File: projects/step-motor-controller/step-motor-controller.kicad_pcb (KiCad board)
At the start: 2 copper layers, 100 x 80 mm, 34 parts, among them J1 Terminal_3P, J2 Motor_4P, J3 Encoder_8P, Q1 BC547, SW1 Limit_SW, SW2 Limit_SW, U1 OKI-78SR-5, U2 UART_4P, U3 ESP32-DevKitC, U4 LV8729, U5 AM26LS32ACN, U6 74HC4050

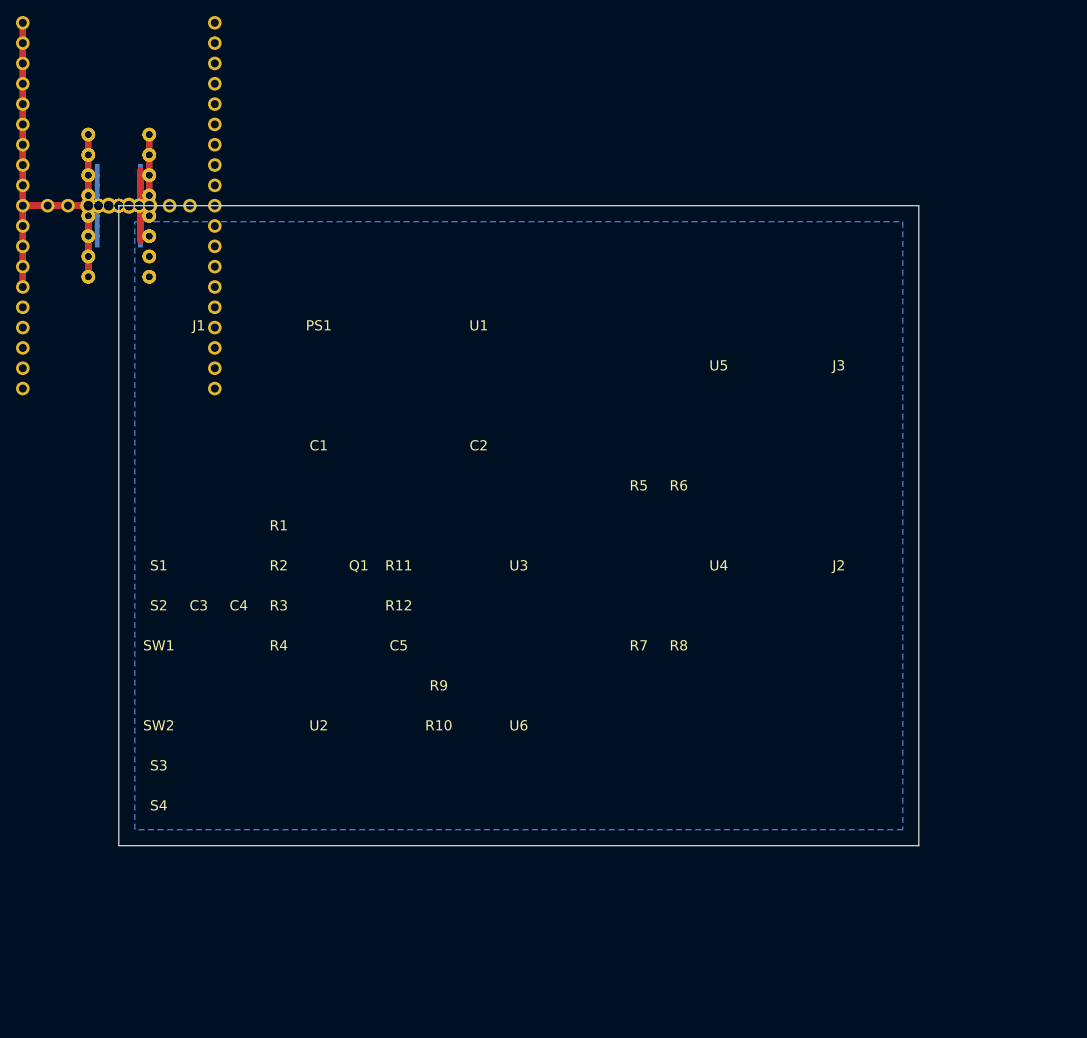
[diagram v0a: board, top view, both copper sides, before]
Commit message: feat: verified Step Motor Controller — 45-net schematic match, routed PCB, 0 electrical DRC, fab package
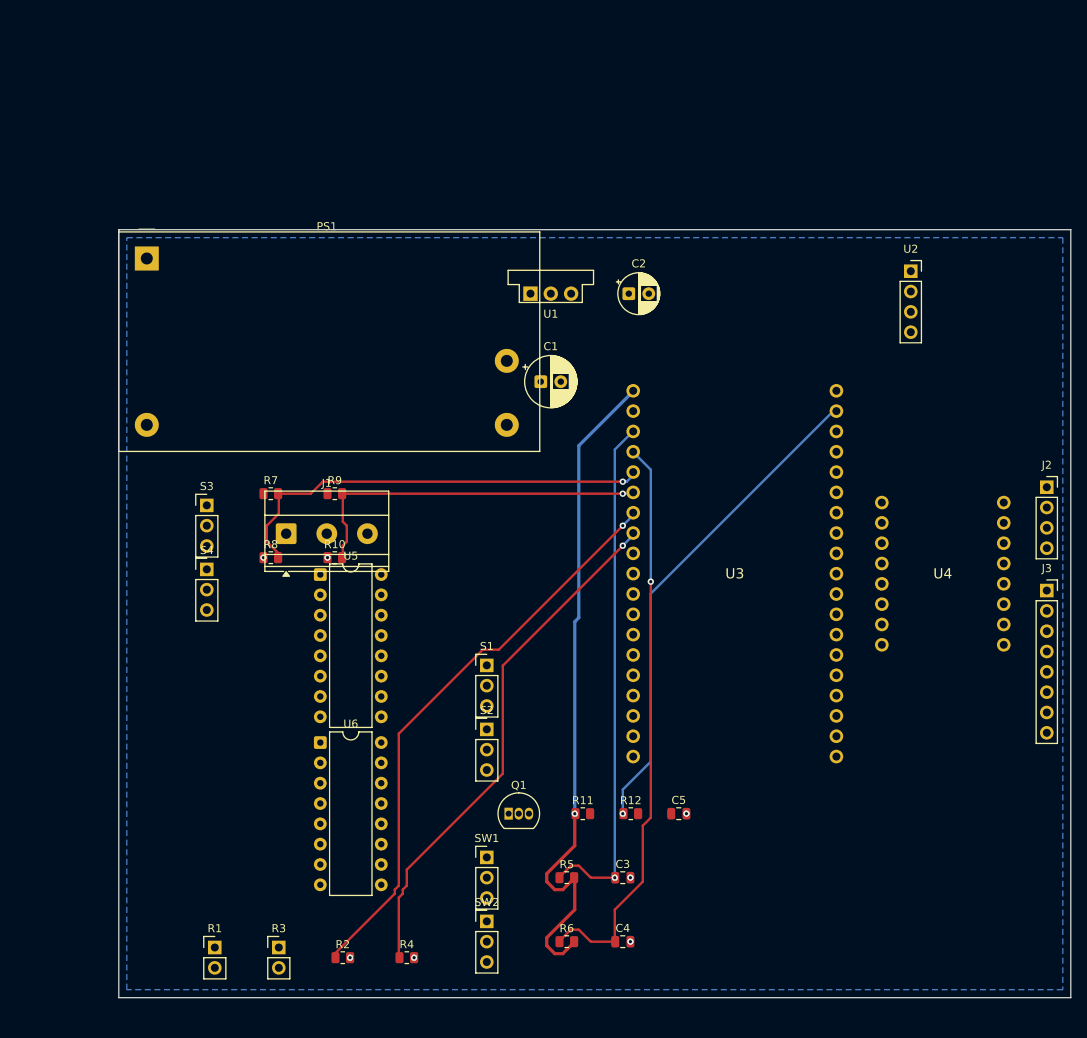
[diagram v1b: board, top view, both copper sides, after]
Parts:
- C1: value 100uF -> C1; footprint (none) -> CP_Radial_D6.3mm_P2.50mm
- C2: value 10uF -> C2; footprint (none) -> CP_Radial_D5.0mm_P2.50mm
- C3: value 100nF -> C3; footprint (none) -> C_0805_2012Metric
- C4: value 100nF -> C4; footprint (none) -> C_0805_2012Metric
- C5: value 100nF -> C5; footprint (none) -> C_0805_2012Metric
- J1: value Terminal_3P -> AC Input; footprint (none) -> TerminalBlock_Phoenix_MKDS-1,5-3-5.08_1x03_P5.08mm_Horizontal
- J2: value Motor_4P -> Motor; footprint (none) -> PinSocket_1x04_P2.54mm_Vertical
- J3: value Encoder_8P -> Encoder; footprint (none) -> PinSocket_1x08_P2.54mm_Vertical
- PS1: footprint (none) -> Converter_ACDC_MeanWell_IRM-20-xx_THT
- Q1: footprint (none) -> TO-92_Inline
- R1: value 10K -> R1; footprint (none) -> PinHeader_1x02_P2.54mm_Vertical
- R10: value 4.7K -> R10; footprint (none) -> R_0805_2012Metric
- R11: value 10K -> R11; footprint (none) -> R_0805_2012Metric
- R12: value 1K -> R12; footprint (none) -> R_0805_2012Metric
- R2: value 10K -> R2; footprint (none) -> R_0805_2012Metric
- R3: value 10K -> R3; footprint (none) -> PinHeader_1x02_P2.54mm_Vertical
- R4: value 10K -> R4; footprint (none) -> R_0805_2012Metric
- R5: value 1K -> R5; footprint (none) -> R_0805_2012Metric
- R6: value 1K -> R6; footprint (none) -> R_0805_2012Metric
- R7: value 10K -> R7; footprint (none) -> R_0805_2012Metric
- R8: value 10K -> R8; footprint (none) -> R_0805_2012Metric
- R9: value 4.7K -> R9; footprint (none) -> R_0805_2012Metric
- S1: value Optical -> S1; footprint (none) -> PinHeader_1x03_P2.54mm_Vertical
- S2: value Optical -> S2; footprint (none) -> PinHeader_1x03_P2.54mm_Vertical
- S3: value Hall -> S3; footprint (none) -> PinHeader_1x03_P2.54mm_Vertical
- S4: value Hall -> S4; footprint (none) -> PinHeader_1x03_P2.54mm_Vertical
- SW1: value Limit_SW -> SW1; footprint (none) -> PinHeader_1x03_P2.54mm_Vertical
- SW2: value Limit_SW -> SW2; footprint (none) -> PinHeader_1x03_P2.54mm_Vertical
- U1: footprint (none) -> Converter_DCDC_Murata_OKI-78SR_Vertical
- U2: value UART_4P -> UART Display; footprint (none) -> PinSocket_1x04_P2.54mm_Vertical
- U5: footprint (none) -> DIP-16_W7.62mm
- U6: value 74HC4050 -> 74HC4050N; footprint (none) -> DIP-16_W7.62mm
- moved U2 93.3 mm to (99.0, 8.19)
- moved C4 63.8 mm to (63.0, 92.0)
- moved C3 63.0 mm to (63.0, 84.0)
- moved R6 58.7 mm to (56.0, 92.0)
- moved U5 56.2 mm to (25.2, 46.1)
- moved R1 53.3 mm to (12.0, 92.7)
- moved R8 52.2 mm to (19.0, 44.0)
- moved R5 49.8 mm to (56.0, 84.0)
- moved R7 49.8 mm to (19.0, 36.0)
- moved R2 49.6 mm to (28.0, 94.0)
- moved SW1 48.8 mm to (46.0, 81.5)
- moved SW2 47.7 mm to (46.0, 89.5)
- moved S2 43.8 mm to (46.0, 65.5)
- moved S1 42.9 mm to (46.0, 57.5)
- moved R3 42.7 mm to (20.0, 92.7)
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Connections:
- C3 pad 1: (no net) -> SW1_SIG
- C3 pad 2: (no net) -> GND
- C4 pad 1: (no net) -> SW2_SIG
- C4 pad 2: (no net) -> GND
- C5 pad 1: (no net) -> CHIP_PU
- C5 pad 2: (no net) -> GND
- J1 pad 1: (no net) -> AC_L
- J1 pad 2: (no net) -> AC_N
- J2 pad 1: (no net) -> MOT_1A
- J2 pad 2: (no net) -> MOT_1B
- J2 pad 3: (no net) -> MOT_2A
- J2 pad 4: (no net) -> MOT_2B
- J3 pad 3: (no net) -> ENC_A_P
- J3 pad 4: (no net) -> ENC_A_N
- J3 pad 5: (no net) -> ENC_B_P
- J3 pad 6: (no net) -> ENC_B_N
- J3 pad 7: (no net) -> ENC_Z_P
- J3 pad 8: (no net) -> ENC_Z_N
- PS1 pad 1: (no net) -> AC_L
- PS1 pad 2: (no net) -> AC_N
- Q1 pad 1: (no net) -> CHIP_PU
- Q1 pad 2: (no net) -> Q1_BASE
- Q1 pad 3: (no net) -> GND
- R1 pad 2: (no net) -> FSR1_TOP
- R10 pad 1: (no net) -> GND
- R10 pad 2: (no net) -> HALL2_DIV
- R11 pad 2: (no net) -> CHIP_PU
- R12 pad 1: (no net) -> GPIO23_RST
- R12 pad 2: (no net) -> Q1_BASE
- R2 pad 1: (no net) -> FSR1_TOP
- R2 pad 2: (no net) -> GND
- R3 pad 2: (no net) -> FSR2_TOP
- R4 pad 1: (no net) -> FSR2_TOP
- R4 pad 2: (no net) -> GND
- R5 pad 1: (no net) -> SW1_SIG
- R6 pad 1: (no net) -> SW2_SIG
- R7 pad 1: (no net) -> HALL1_RAW
- R7 pad 2: (no net) -> HALL1_DIV
- R8 pad 1: (no net) -> GND
- R8 pad 2: (no net) -> HALL1_DIV
- R9 pad 1: (no net) -> HALL2_RAW
- R9 pad 2: (no net) -> HALL2_DIV
- S1 pad 2: (no net) -> OPTIC1_RAW
- S1 pad 3: (no net) -> GND
- S2 pad 2: (no net) -> OPTIC2_RAW
- S2 pad 3: (no net) -> GND
- S3 pad 2: (no net) -> GND
- S3 pad 3: GND -> HALL1_RAW
- S4 pad 2: (no net) -> GND
- S4 pad 3: GND -> HALL2_RAW
- SW1 pad 1: (no net) -> SW1_SIG
- SW1 pad 2: (no net) -> GND
- SW1 pad 3: GND -> (no net)
- SW2 pad 1: (no net) -> SW2_SIG
- SW2 pad 2: (no net) -> GND
- SW2 pad 3: GND -> (no net)
- U2 pad 2: (no net) -> UART_M_TX
- U2 pad 3: (no net) -> UART_M_RX
- U3 pad 10: (no net) -> M_STEP
- U3 pad 11: (no net) -> M_DIR
- U3 pad 12: (no net) -> M_EN
- U3 pad 15: (no net) -> ENC_Z_ESP
- U3 pad 19: (no net) -> +5V
- U3 pad 2: (no net) -> CHIP_PU
- U3 pad 26: (no net) -> M_MS1
- U3 pad 27: (no net) -> UART_M_TX
- U3 pad 28: (no net) -> UART_M_RX
- U3 pad 29: (no net) -> M_MS2
- U3 pad 3: (no net) -> SW1_SIG
- U3 pad 30: (no net) -> GPIO18_OPTIC1
- U3 pad 31: (no net) -> GPIO19_OPTIC2
- U3 pad 32: (no net) -> GPIO21_ENC_A
- U3 pad 33: (no net) -> GPIO22_ENC_B
- U3 pad 37: (no net) -> GPIO23_RST
- U3 pad 4: (no net) -> SW2_SIG
- U3 pad 5: (no net) -> HALL1_DIV
- U3 pad 6: (no net) -> HALL2_DIV
- U3 pad 7: (no net) -> FSR1_TOP
- U3 pad 8: (no net) -> FSR2_TOP
- U3 pad 9: (no net) -> M_MS3
- U4 pad 1: (no net) -> M_EN
- U4 pad 11: (no net) -> MOT_2B
- U4 pad 12: (no net) -> MOT_2A
- U4 pad 13: (no net) -> MOT_1B
- U4 pad 14: (no net) -> MOT_1A
- U4 pad 2: (no net) -> M_MS1
- U4 pad 3: (no net) -> M_MS2
- U4 pad 4: (no net) -> M_MS3
- U4 pad 7: (no net) -> M_STEP
- U4 pad 8: (no net) -> M_DIR
- U5 pad 1: (no net) -> ENC_A_N
- U5 pad 10: (no net) -> ENC_Z_N
- U5 pad 11: (no net) -> ENC_Z_BUF
- U5 pad 2: (no net) -> ENC_A_P
- U5 pad 3: (no net) -> ENC_A_BUF
- U5 pad 5: (no net) -> ENC_B_BUF
- U5 pad 6: (no net) -> ENC_B_N
- U5 pad 7: (no net) -> ENC_B_P
- U5 pad 9: (no net) -> ENC_Z_P
- U6 pad 10: (no net) -> GPIO18_OPTIC1
- U6 pad 11: (no net) -> OPTIC2_RAW
- U6 pad 12: (no net) -> GPIO19_OPTIC2
- U6 pad 2: (no net) -> GPIO21_ENC_A
- U6 pad 3: (no net) -> ENC_A_BUF
- U6 pad 4: (no net) -> GPIO22_ENC_B
- U6 pad 5: (no net) -> ENC_B_BUF
- U6 pad 6: (no net) -> ENC_Z_ESP
- U6 pad 7: (no net) -> ENC_Z_BUF
- U6 pad 9: (no net) -> OPTIC1_RAW
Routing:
- net GND: track 100.0 -> 0.00 mm, vias 0 -> 7
- net +5V: track 80.8 -> 0.00 mm
- net FSR1_TOP: track 0.00 -> 72.2 mm, vias 0 -> 1
- net SW2_SIG: track 0.00 -> 71.9 mm, vias 0 -> 1
- net SW1_SIG: track 0.00 -> 65.3 mm, vias 0 -> 1
- net FSR2_TOP: track 0.00 -> 65.2 mm, vias 0 -> 1
- net GPIO23_RST: track 0.00 -> 61.5 mm, vias 0 -> 1
- net HALL1_DIV: track 0.00 -> 54.8 mm, vias 0 -> 1
- net +3V3: track 37.9 -> 85.1 mm, vias 0 -> 1
- net HALL2_DIV: track 0.00 -> 44.9 mm, vias 0 -> 1
- net +24V: track 17.3 -> 0.00 mm
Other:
- board size 100 x 80 mm -> 119 x 96 mm

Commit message: feat: THT PCB - routed, 0 electrical DRC, 0 parity, Gerber+drill+BOM+PnP+renders
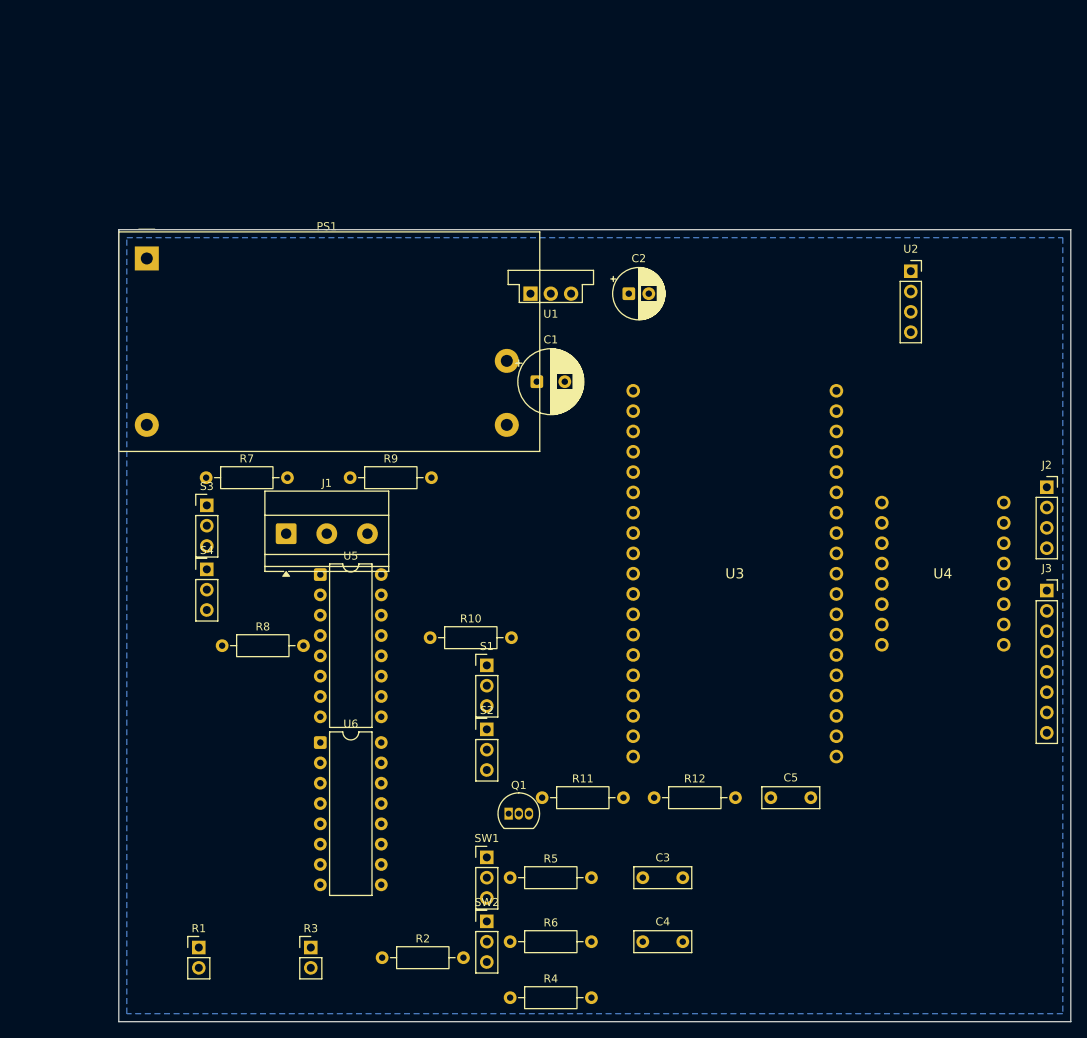
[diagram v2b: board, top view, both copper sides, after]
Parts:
- C1: footprint CP_Radial_D6.3mm_P2.50mm -> CP_Radial_D8.0mm_P3.50mm
- C2: footprint CP_Radial_D5.0mm_P2.50mm -> CP_Radial_D6.3mm_P2.50mm
- C3, C4, C5: footprint C_0805_2012Metric -> C_Rect_L7.0mm_W2.5mm_P5.00mm
- R10, R11, R12, R2, R4, R5, R6, R7, R8, R9: footprint R_0805_2012Metric -> R_Axial_DIN0207_L6.3mm_D2.5mm_P10.16mm_Horizontal
- moved R10 15.6 mm to (38.9, 54.0)
- moved R4 13.9 mm to (48.9, 99.0)
- moved R8 12.6 mm to (12.9, 55.0)
- moved C5 11.7 mm to (81.5, 74.0)
- moved R7 8.32 mm to (10.9, 34.0)
- moved R5 7.08 mm to (48.9, 84.0)
- moved R6 7.08 mm to (48.9, 92.0)
- moved R11 5.46 mm to (52.9, 74.0)
- moved R2 4.92 mm to (32.9, 94.0)
- moved R3 4.00 mm to (24.0, 92.7)
- moved R12 3.54 mm to (66.9, 74.0)
- moved R9 2.77 mm to (28.9, 34.0)
- moved C3 2.50 mm to (65.5, 84.0)
- moved C4 2.50 mm to (65.5, 92.0)
- moved R1 2.00 mm to (10.0, 92.7)
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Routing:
- net +3V3: track 85.1 -> 0.00 mm, vias 1 -> 0
- net FSR1_TOP: track 72.2 -> 0.00 mm, vias 1 -> 0
- net SW2_SIG: track 71.9 -> 0.00 mm, vias 1 -> 0
- net SW1_SIG: track 65.3 -> 0.00 mm, vias 1 -> 0
- net FSR2_TOP: track 65.2 -> 0.00 mm, vias 1 -> 0
- net GPIO23_RST: track 61.5 -> 0.00 mm, vias 1 -> 0
- net HALL1_DIV: track 54.8 -> 0.00 mm, vias 1 -> 0
- net HALL2_DIV: track 44.9 -> 0.00 mm, vias 1 -> 0
- net GND: vias 7 -> 0
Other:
- board size 119 x 96 mm -> 119 x 99 mm
